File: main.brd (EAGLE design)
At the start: 78 x 235 mm, 111 parts, among them IC10 FGPMMOPA6H, IC2 25LC1024-I/P, IC6 MPL3115A2LGA, IC7 FXAS21000, IC8 ADXL343BCCZ, Q1 12MHz, Q2 MCP9700A-E/TO, Q3 FQP7P06, Q4 MCP9700A-E/TO, U1 ATMEGA1284P-PU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

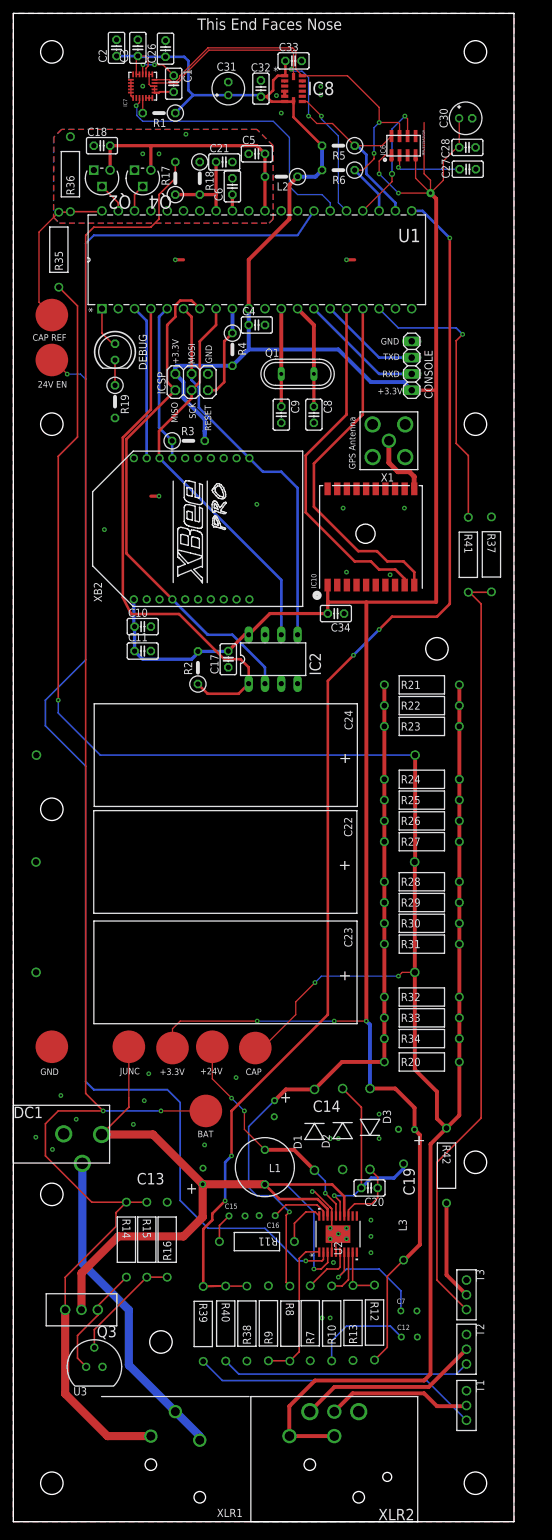
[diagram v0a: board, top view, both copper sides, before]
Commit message: Added terminal pads
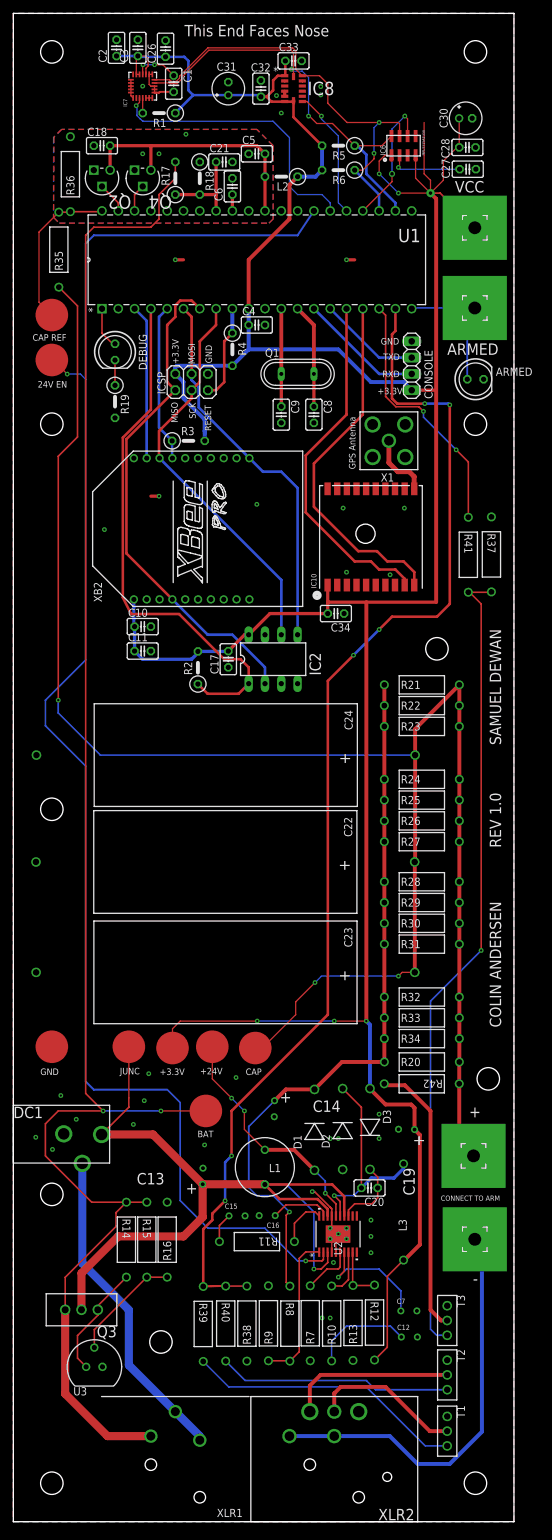
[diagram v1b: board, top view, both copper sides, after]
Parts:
- added ARMED: (no value), led:LED5MM
- added PAD1, PAD2, PAD3, PAD6: (no value), Power:3,81/1,4
- moved R42 21.0 mm to (57.8, 68.2), turned to 180 degrees
- moved T1 5.00 mm to (67.6, 14.1)
- moved T2 5.00 mm to (67.6, 22.9)
- moved T3 5.00 mm to (67.6, 31.4)
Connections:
- removed net DROGUE_TRIGGER: U1.20
- new net ARMED_SENSE: ARMED.A, PAD3.1, U1.20
- new net N$31: PAD6.1, XLR2.1, XLR2.3
- net ENGINE_VALVE: now also U1.21; no longer U1.19
- net GND: now also ARMED.K
- net MAIN_TRIGGER: now also U1.19; no longer U1.21
- net N$81: now also PAD2.1; no longer XLR2.1, XLR2.3
- net VCC: now also PAD1.1
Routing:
- net N$81: track 363.2 -> 280.0 mm
- net N$31: track 0.00 -> 64.3 mm
- net N$75: track 15.6 -> 43.3 mm
- net ARMED_SENSE: track 0.00 -> 21.5 mm
- net MAIN_TRIGGER: track 201.6 -> 191.3 mm, vias 5 -> 6
- net VCC: track 491.7 -> 500.9 mm
- net N$82: track 121.2 -> 125.7 mm, vias 0 -> 1
- net CAP_DISCHARGE: track 44.4 -> 40.4 mm, vias 1 -> 2
- net N$80: track 39.0 -> 36.4 mm
- net N$78: track 28.4 -> 26.1 mm
- net N$79: track 44.8 -> 43.5 mm
- net N$77: track 22.6 -> 23.7 mm
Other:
- board text added: "+"
- board text added: "-"
- board text added: "ARMED"
- board text added: "COLIN ANDERSEN"
- board text added: "CONNECT TO ARM"
- board text added: "REV 1.0"
- board text added: "SAMUEL DEWAN"
- board text added: "VCC"
